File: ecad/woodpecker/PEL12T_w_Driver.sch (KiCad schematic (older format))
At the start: 14 parts, among them Q1 BSS138, SW2 PEL12T, U2 TLC5973

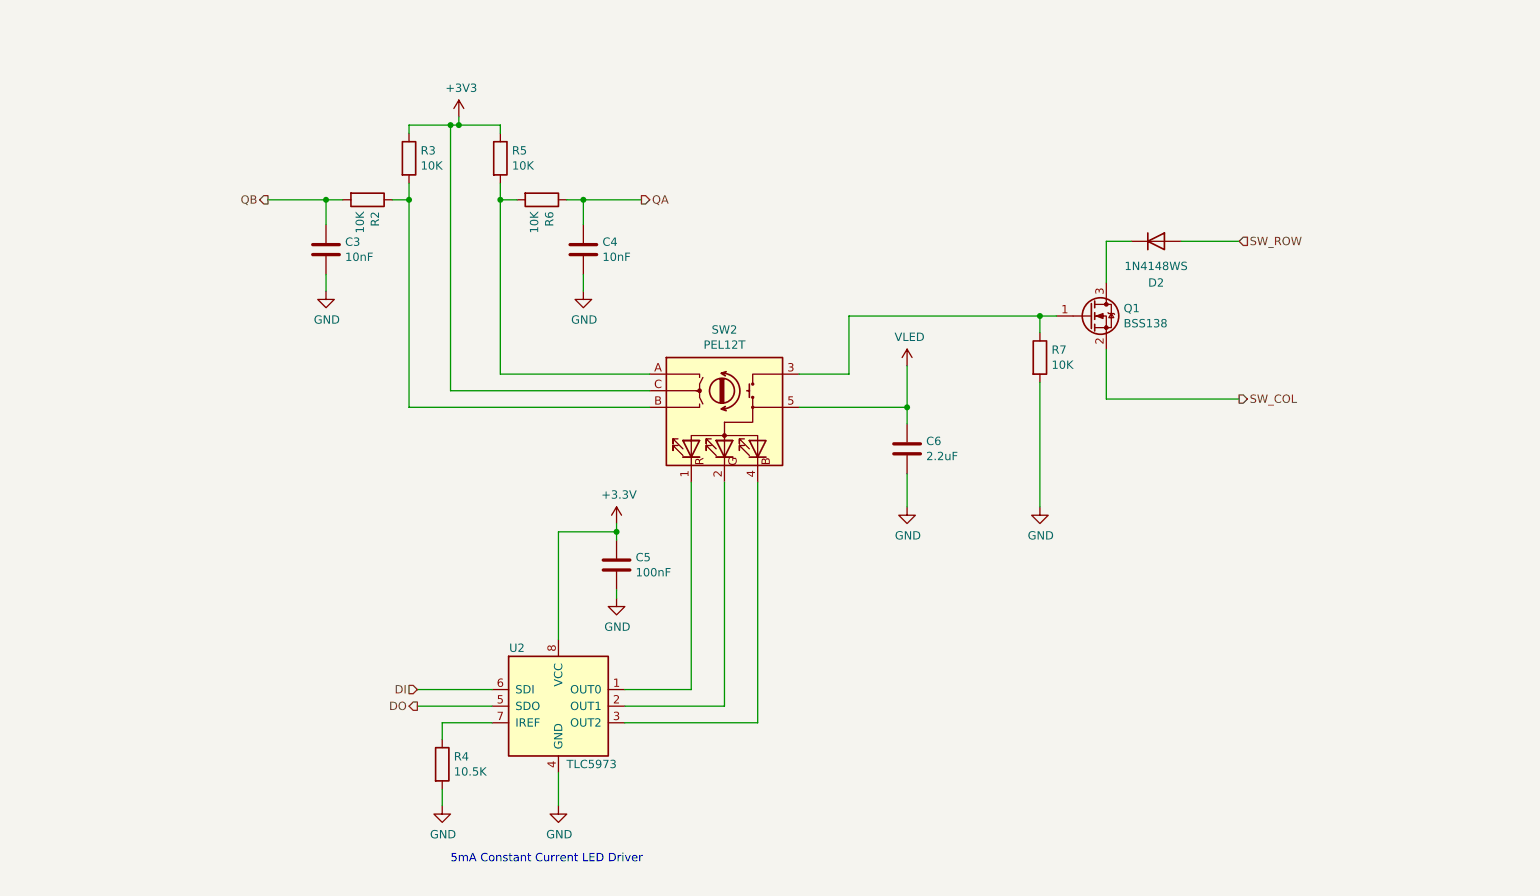
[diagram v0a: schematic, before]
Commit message: Adds bottom section in monolithic design
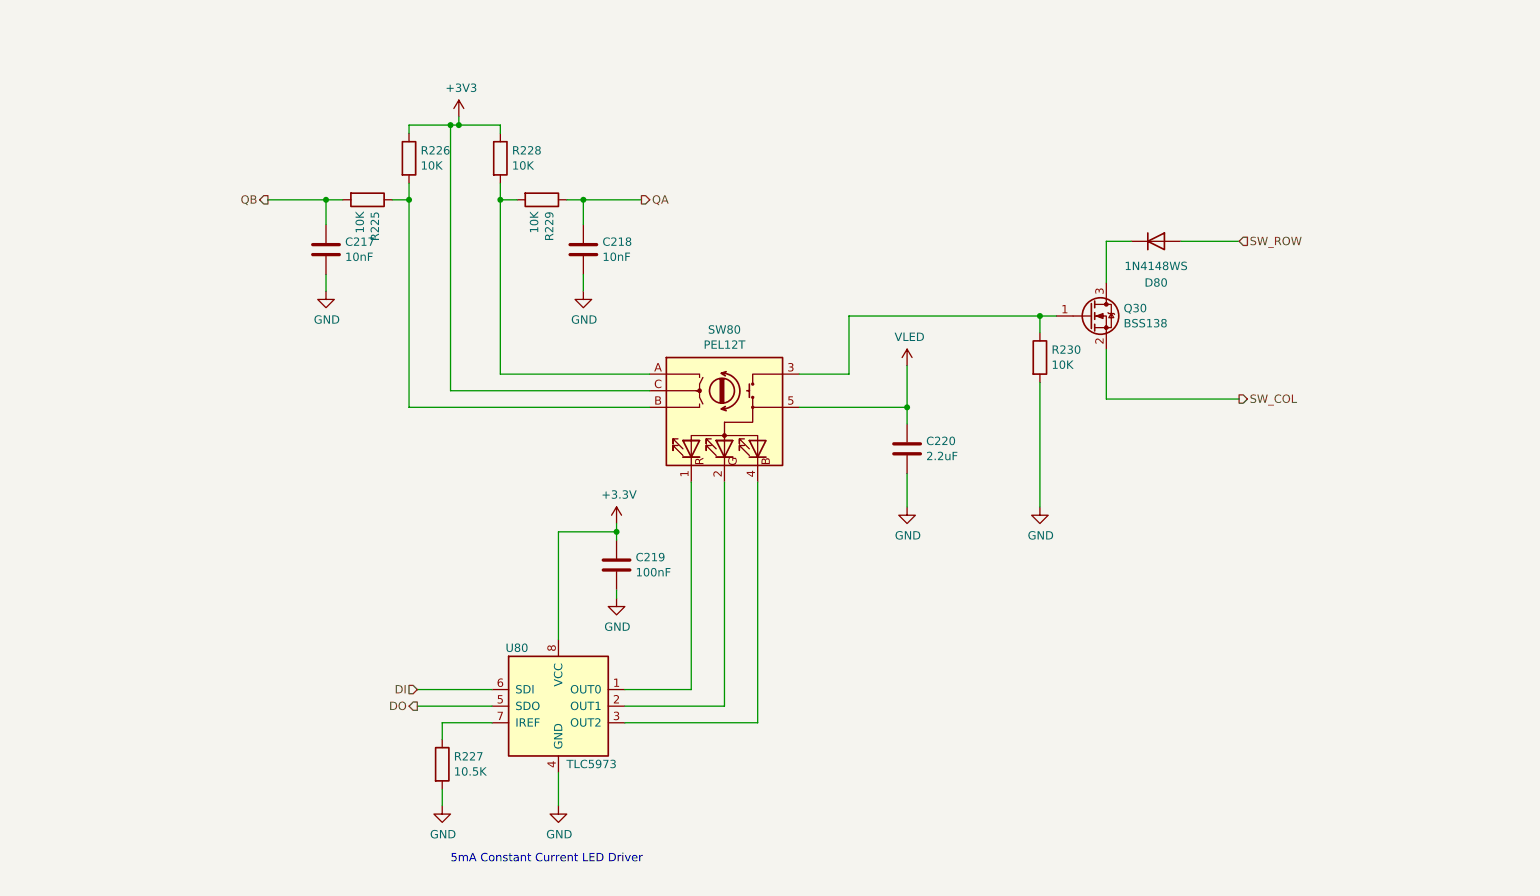
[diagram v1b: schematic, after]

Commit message: Corrects Quadrature encoder debounce circuit on put them on the scan matrix
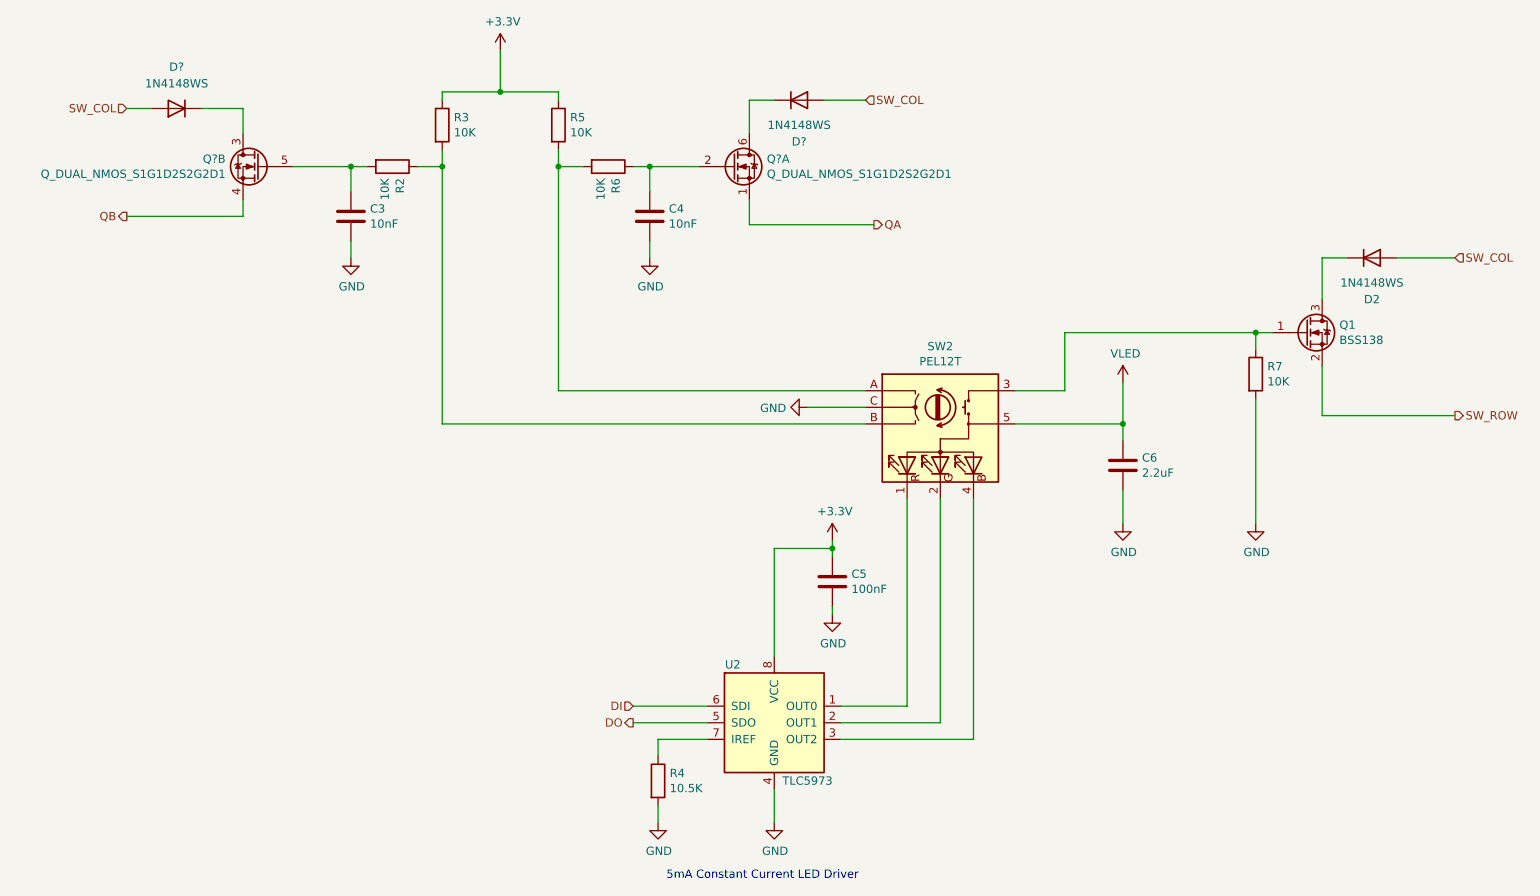
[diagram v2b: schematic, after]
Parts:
- added D? (x2): 1N4148WS, Diode_SMD:D_SOD-323_HandSoldering, symbol Diode:1N4148WS
- added Q? (x2): Q_DUAL_NMOS_S1G1D2S2G2D1, symbol Device:Q_DUAL_NMOS_S1G1D2S2G2D1
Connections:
- net +3V3: no longer SW2.C
- net GND: now also SW2.C
- net QA: now also Q?.1 (S); no longer C4.1, R6.1
- net QB: now also Q?.4 (S); no longer C3.1, R2.2
- net SW_COL: now also D2.2 (A), D?.2 (A), D?.2 (A); no longer Q1.2 (S)
- net SW_ROW: now also Q1.2 (S); no longer D2.2 (A)
- new net: D?.1 (K), Q?.6 (D)
- new net: D?.1 (K), Q?.3 (D)
- new net: C3.1, Q?.5 (G), R2.2
- new net: C4.1, Q?.2 (G), R6.1
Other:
- moved on the sheet: C3, C4, C5, C6, D2, Q1, R2, R3, R4, R5, R6, R7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

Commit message: Implemented Top Section Revision A
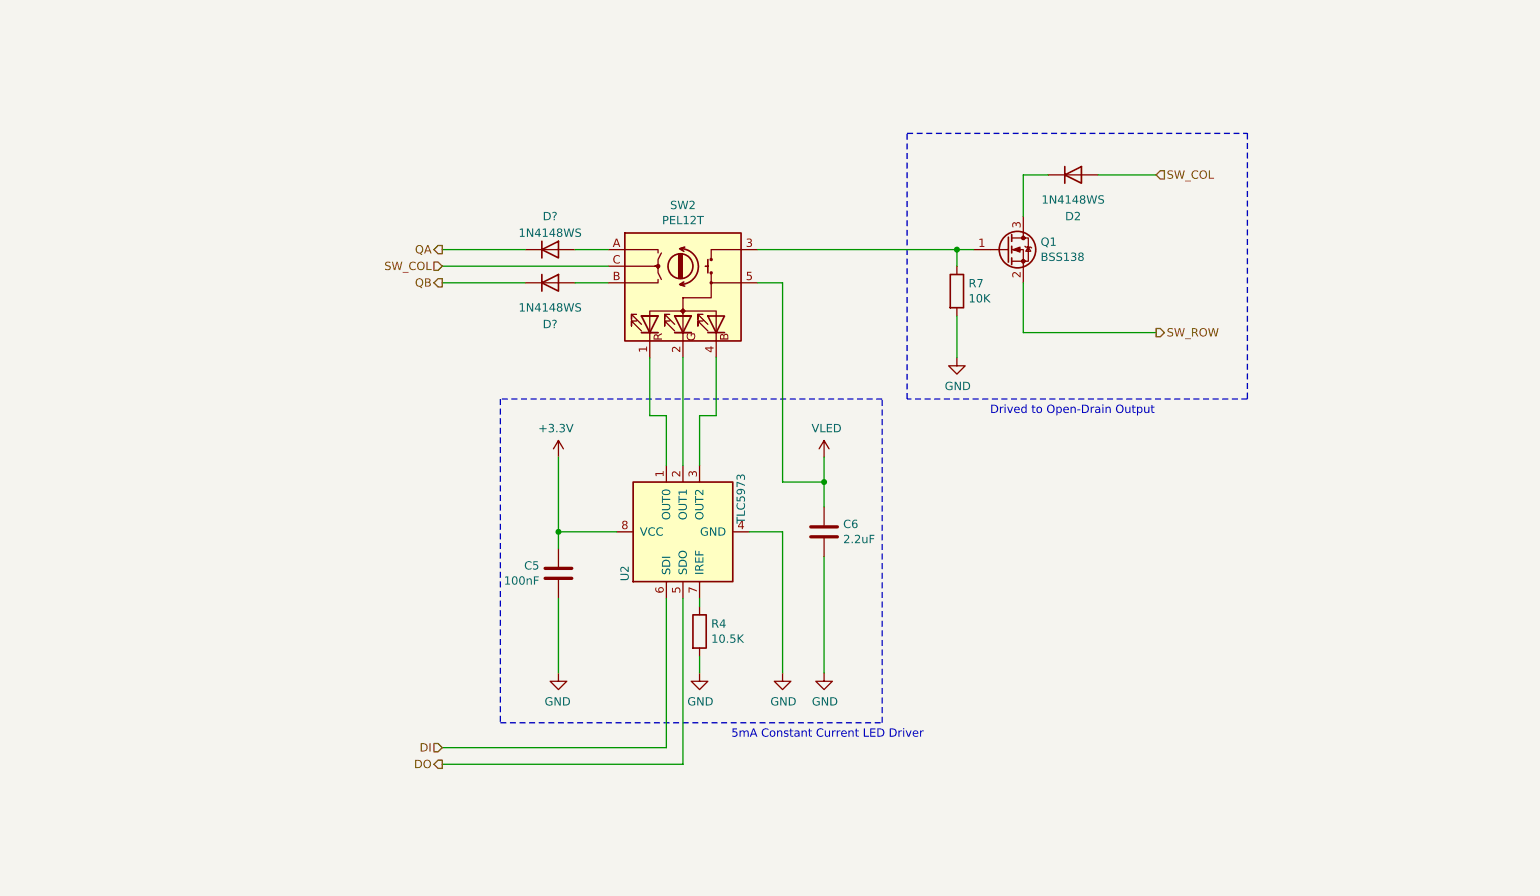
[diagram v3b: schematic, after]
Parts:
- removed C3, C4: 10nF, Capacitor_SMD:C_0603_1608Metric_Pad1.08x0.95mm_HandSolder, symbol Device:C
- removed Q? (x2): Q_DUAL_NMOS_S1G1D2S2G2D1, symbol Device:Q_DUAL_NMOS_S1G1D2S2G2D1
- removed R2, R3, R5, R6: 10K, Resistor_SMD:R_0603_1608Metric_Pad0.98x0.95mm_HandSolder, symbol Device:R
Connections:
- net GND: no longer SW2.C
- net QA: now also D?.1 (K)
- net QB: now also D?.1 (K)
- net SW_COL: now also SW2.C; no longer D?.2 (A), D?.2 (A)
- net at SW2.A: now also D?.2 (A)
- net at SW2.B: now also D?.2 (A)
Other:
- note added: "Drived to Open-Drain Output"
- moved on the sheet: C5, C6, D2, D?, Q1, R4, R7, SW2, U2
